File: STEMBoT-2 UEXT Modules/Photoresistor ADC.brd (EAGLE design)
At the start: 21.6 x 27.6 mm, 18 parts, among them IC1 74HC165PW,118, IC2 LMV324DR2G, IC3 LMV324DR2G, Q1 MMBT3904LP-7

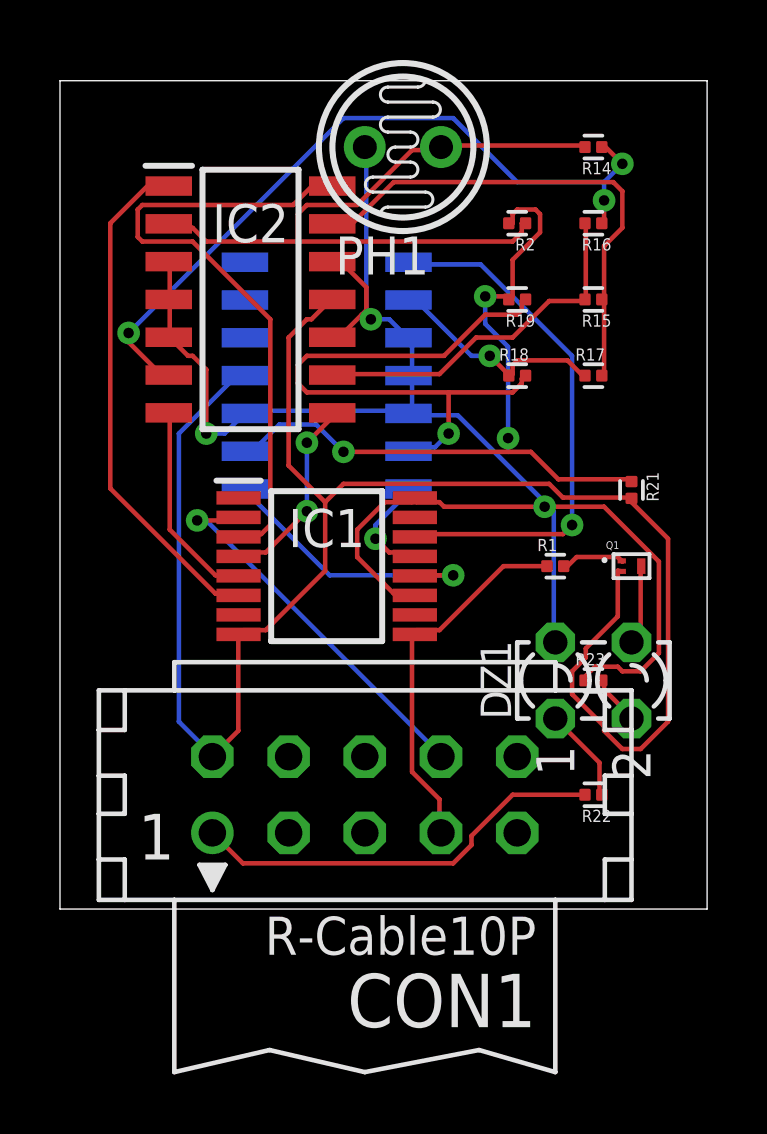
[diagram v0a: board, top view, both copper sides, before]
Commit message: Adjusted ADC modules for PCB order. Dan, these are auto-routed.
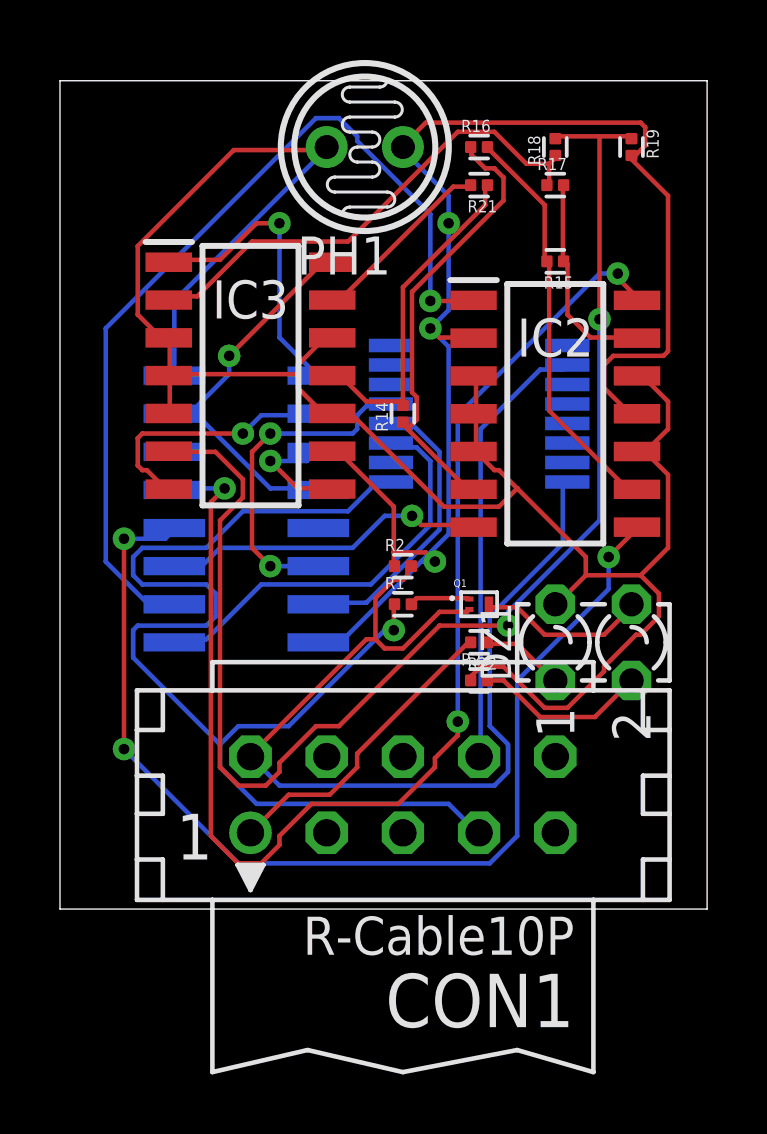
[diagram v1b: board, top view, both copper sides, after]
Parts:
- added U1: SN74HC148D, SN74HC148D:SOIC127P600X175-16N
- moved R2 12.0 mm to (11.4, 11.4), turned to 0 degrees
- moved R21 11.4 mm to (14.0, 24.1), turned to 180 degrees
- moved R14 10.9 mm to (11.4, 16.5), turned to 90 degrees
- moved IC2 10.9 mm to (16.5, 16.5)
- moved R18 7.73 mm to (16.5, 25.4), turned to 90 degrees
- moved IC1 7.18 mm to (14.0, 16.5), flipped to the bottom
- moved R17 6.48 mm to (16.5, 24.1)
- moved R22 6.35 mm to (14.0, 8.89)
- moved R19 6.35 mm to (19.1, 25.4), turned to 270 degrees
- moved R1 5.24 mm to (11.4, 10.2)
- moved Q1 5.24 mm to (14.0, 10.2)
- moved R16 4.58 mm to (14.0, 25.4), turned to 0 degrees
- moved R23 3.81 mm to (14.0, 7.62)
- moved IC3 2.54 mm to (6.35, 17.8), flipped to the top
- moved R15 1.80 mm to (16.5, 21.6)
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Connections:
- removed net N$17: IC3.9, R19.2, R2.2, R21.1
- removed net N$32: IC1.5, IC2.7
- removed net N$6 (its old number): IC1.12, IC3.8
- removed net N$7 (its old number): DZ1.K1, IC1.11, IC1.16, IC2.10, IC2.12, IC2.3, IC2.4, IC2.5, IC3.10, IC3.3, IC3.4, IC3.5, PH1.1, R23.1
- new net N$12: DZ1.K1, IC2.10, IC2.12, IC2.3, IC2.4, IC2.5, IC3.10, IC3.12, IC3.3, IC3.4, IC3.5, PH1.1, R23.1, U1.16
- new net N$15: IC3.13, R21.2
- new net N$16: IC3.14, U1.15, U1.4
- new net N$19: IC1.11, U1.9
- new net N$20: IC1.12, U1.7
- new net N$21: IC1.13, U1.6
- new net N$22: CON1.2, IC1.8, Q1.2, R2.2
- new net N$8: IC2.11, IC2.2, IC3.11, IC3.9, PH1.2, R14.2, R19.2, R2.1, R21.1, U1.8
- net N$11: now also IC3.8, U1.3; no longer IC2.2, PH1.2, R14.2, R2.1
- net N$2: now also IC2.7, U1.11; no longer CON1.2, IC1.8, IC2.11, IC3.11, Q1.2, R21.2
- net N$23: now also U1.2; no longer IC1.13
- net N$26: now also U1.1; no longer IC1.14
- net N$30: now also U1.13; no longer IC1.3
- net N$31: now also U1.12; no longer IC1.4
- net N$33: now also U1.10; no longer IC1.6
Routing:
- net N$12: track 0.00 -> 70.3 mm
- net N$8: track 0.00 -> 61.4 mm, vias 0 -> 3
- net N$7 (its old number): track 59.3 -> 0.00 mm, vias 3 -> 0
- net N$2: track 60.6 -> 10.8 mm, vias 0 -> 1
- net N$22: track 0.00 -> 33.0 mm
- net N$31: track 6.58 -> 35.9 mm, vias 2 -> 3
- net N$7: track 12.5 -> 40.5 mm, vias 0 -> 1
- net N$17: track 25.2 -> 0.00 mm, vias 3 -> 0
- net N$9: track 20.3 -> 45.2 mm, vias 1 -> 2
- net N$30: track 21.3 -> 43.3 mm, vias 0 -> 3
- net N$11: track 24.1 -> 4.17 mm, vias 0 -> 1
- net N$19: track 0.00 -> 13.9 mm
- net N$16: track 0.00 -> 13.7 mm, vias 0 -> 1
- net N$33: track 17.1 -> 30.2 mm, vias 0 -> 1
- net N$21: track 0.00 -> 11.2 mm, vias 0 -> 2
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
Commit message: Once again, updating ADC shematics and boards. Used autorouter.
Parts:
- removed IC2, IC3: LMV324DR2G, LMV324DR2G:SOP126P600X175-14N
- added R3: ERJ-1RHD3601C, Resistor:RESC0603X26N
- added U2, U3: MAX964ESET, MAX964ESET:SOIC127P600X175-16N
- moved U1 1.27 mm to (2.54, 8.89)
- flipped R15 to the bottom, turned to 90 degrees
- flipped R16 to the bottom, turned to 270 degrees
- flipped R17 to the bottom, turned to 90 degrees
- flipped R18 to the bottom
- flipped R19 to the bottom, turned to 90 degrees
- flipped R21 to the bottom, turned to 270 degrees
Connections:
- removed net N$2: IC2.7, U1.11
- removed net N$30: IC2.14, U1.13
- removed net N$31: IC2.8, U1.12
- removed net N$33: IC2.1, U1.10
- new net N$17: U1.3, U2.14
- new net N$18: U1.2, U2.11
- new net N$27: U1.12, U3.14
- new net N$28: U1.11, U3.11
- new net N$29: U1.10, U3.10
- new net VCC: U3.13
- net N$10: now also R17.2, U2.7; no longer IC2.6, R14.1
- net N$11: now also R17.1, R21.2, U3.1; no longer IC3.8, U1.3
- net N$12: now also R3.2, U2.12, U2.13; no longer IC2.10, IC2.12, IC2.3, IC2.4, IC2.5, IC3.10, IC3.12, IC3.3, IC3.4, IC3.5
- net N$13: now also R18.1, R21.1, U3.3; no longer IC2.9, R15.2, R16.2
- net N$14: now also R18.2, R19.2, U3.5; no longer IC2.13, R15.1, R17.2
- net N$15: now also PH1.2, R19.1, R2.1, U2.2, U2.4, U2.6, U2.8, U3.12, U3.2, U3.4, U3.6, U3.7, U3.8; no longer IC3.13, R21.2
- net N$16: now also U2.15; no longer IC3.14, U1.15
- net N$22: now also U1.8
- net N$23: now also U1.13, U2.10; no longer IC3.7, U1.2
- net N$26: now also U3.15; no longer IC3.1
- net N$3: now also R15.2, R16.2, U2.5; no longer IC3.2, R17.1, R18.1
- net N$8: now also R3.1, U2.1; no longer IC2.11, IC2.2, IC3.11, IC3.9, PH1.2, R19.2, R2.1, R21.1, U1.8
- net N$9: now also R14.1, R15.1, U2.3; no longer IC3.6, R18.2, R19.1
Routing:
- net N$15: track 6.21 -> 94.8 mm, vias 0 -> 1
- net N$30: track 43.3 -> 0.00 mm, vias 3 -> 0
- net N$29: track 0.00 -> 40.7 mm, vias 0 -> 3
- net N$31: track 35.9 -> 0.00 mm, vias 3 -> 0
- net N$8: track 61.4 -> 30.0 mm, vias 3 -> 1
- net N$33: track 30.2 -> 0.00 mm, vias 1 -> 0
- net N$27: track 0.00 -> 29.2 mm, vias 0 -> 1
- net N$18: track 0.00 -> 28.1 mm, vias 0 -> 1
- net N$9: track 45.2 -> 21.3 mm
- net N$28: track 0.00 -> 20.0 mm, vias 0 -> 3
- net N$7: track 40.5 -> 24.6 mm, vias 1 -> 3
- net N$12: track 70.3 -> 55.1 mm, vias 0 -> 2
- net N$11: track 4.17 -> 15.8 mm
- net N$2: track 10.8 -> 0.00 mm, vias 1 -> 0
- net N$10: track 14.9 -> 25.7 mm, vias 0 -> 1
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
